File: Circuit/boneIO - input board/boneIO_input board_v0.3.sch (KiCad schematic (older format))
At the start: 274 parts, among them J1 Conn_02x04_Odd_Even, J10 Screw_Terminal_01x04, J11 Screw_Terminal_01x08, J12 BeagleBone_Black_Header, J13 ZW_VCC, J14 ZW_GND, J15 BeagleBone_Black_Header, J16 INNY ZASILACZ, J2 Screw_Terminal_01x08, J3 Screw_Terminal_01x08, J4 Screw_Terminal_01x08, J5 Screw_Terminal_01x08, J6 Screw_Terminal_01x08, J7 Screw_Terminal_01x08, J8 Screw_Terminal_01x08, J9 Screw_Terminal_01x08, SW1 SW_Push, U1 EL357N-G, U1 P82B96, U16 DS1307Z+, U17 TLP290-4, U6 LM2596S-ADJ, U7 RS485, Y1 32,788 MHz

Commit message: PCB design work
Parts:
- removed C55, C56, C57, C58: 100n, Capacitor_SMD:C_0603_1608Metric, symbol Device:C
- removed R108, R109, R110, R111: 4,7k, Resistor_SMD:R_0603_1608Metric, symbol Device:R
- removed R113, R114, R115, R116: 10k, Resistor_SMD:R_0603_1608Metric, symbol Device:R
- removed U17: TLP290-4, Package_SO:SOP-16_4.55x10.3mm_P1.27mm, symbol Isolator:TLP290-4
- U12, U13, U14, U15, U16, U17, U18, U19, U20, U21, U22, U23, U24, U25, U26, U27, U28, U29, U3, U30, U31, U32, U33, U34, U35, U37, U38, U39, U4, U40, U41, U42, U43, U44, U45, U46, U47, U48, U49, U5, U50, U51, U52, U53, U54, U55, U56, U6, U7, U8, U9: renamed from U?; value EL357N-G -> PC817X2NIP0F; footprint Package_SO:OPTO_EL357N-G -> boneIO - RM85:SOT254P975X400-4N
- U2: renamed from U1; value EL357N-G -> PC817X2NIP0F; footprint Package_SO:OPTO_EL357N-G -> boneIO - RM85:SOT254P975X400-4N
- gave numbers to parts that had none: 153
- renumbered C20 to C12, C21 to C13, C38 to C22, C22 to C4, J3 to J1, J2 to J10, J13 to J12, J14 to J13, J16 to J14, J12 to J15, J15 to J16, J4 to J2, J5 to J3, J6 to J4, J7 to J5, J8 to J6, J9 to J7, J10 to J8, J1 to J9, R26 to R10, R18 to R11, R35 to R19, R36 to R20, R37 to R29, R70 to R38, R71 to R39, R92 to R56, R97 to R57, R106 to R66, R107 to R67, R112 to R76, R17 to R9, U6 to U10, U7 to U11, U16 to U36
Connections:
- wire segments 954 -> 910
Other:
- moved on the sheet: ANVDD1, BT1, C1, C10, C11, C12, C13, C14, C15, C16, C17, C18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

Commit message: update PCB
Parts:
- J15, J16: symbol Connector_Generic:BeagleBone_Black_Header -> boneIO_input-board_v0.3-rescue:BeagleBone_Black_Header-Connector_Generic
- U11: symbol RF_Module:RS485 -> boneIO_input-board_v0.3-rescue:RS485-RF_Module
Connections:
- net P9,25 is gone; now on net P9.25: C42.1, R88.1, U40.4
- net P9.29_OUT: now also J6.7 (Pin_7); no longer J6.8 (Pin_8)
- net P9.30_OUT: now also J6.8 (Pin_8); no longer J6.7 (Pin_7)
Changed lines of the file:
@@
 P8.07_OUT
 $Comp
-L RF_Module:RS485 U11
+L boneIO_input-board_v0.3-rescue:RS485-RF_Module U11
 U 1 1 6187A9D0
 P 6350 4700
@@
 P8.39_OUT
 $Comp
-L Connector_Generic:BeagleBone_Black_Header J15
+L boneIO_input-board_v0.3-rescue:BeagleBone_Black_Header-Connector_Generic J15
 U 1 1 64765995
 P 27900 3650
@@
 $EndComp
 $Comp
-L Connector_Generic:BeagleBone_Black_Header J16
+L boneIO_input-board_v0.3-rescue:BeagleBone_Black_Header-Connector_Generic J16
 U 1 1 643393F0
 P 29900 3650
@@
 Text GLabel 6450 9100 2    50   Input ~ 0
 P9.31_OUT
-Text GLabel 6450 9200 2    50   Input ~ 0
-P9.30_OUT
 Text GLabel 6450 9300 2    50   Input ~ 0
+P9.30_OUT
+Text GLabel 6450 9200 2    50   Input ~ 0
 P9.29_OUT
 Text GLabel 8050 7600 2    50   Input ~ 0
@@
 $EndComp
 Text GLabel 17700 15900 2    50   Input ~ 0
-P9,25
+P9.25
 Wire Wire Line
 	16850 15900 17350 15900

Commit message: update PCB 08/11/21
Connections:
- net P9.07 is gone; now on net P8.07: C55.1, R113.1, U53.4
- net P9.24 is gone; now on net P8.13: C51.1, R105.1, U49.4
- net P9.26 is gone; now on net P8.19: C41.1, R87.1, U39.4
- net P8.07_OUT: now also J8.4 (Pin_4); no longer J6.4 (Pin_4)
- net P8.08_OUT: now also J8.3 (Pin_3), U31.2; no longer J6.3 (Pin_3), U35.2
- net P8.09_OUT: now also J8.2 (Pin_2), U32.2; no longer J6.2 (Pin_2), U34.2
- net P8.10_OUT: now also J6.8 (Pin_8); no longer J4.8 (Pin_8)
- net P8.11_OUT: now also J6.7 (Pin_7), U34.2; no longer J4.7 (Pin_7), U32.2
- net P8.12_OUT: now also J6.6 (Pin_6), U35.2; no longer J4.6 (Pin_6), U31.2
- net P8.14_OUT: now also J6.4 (Pin_4), U26.2; no longer J4.5 (Pin_5), U30.2
- net P8.15_OUT: now also J6.3 (Pin_3), U27.2; no longer J4.4 (Pin_4), U29.2
- net P8.16_OUT: now also J6.2 (Pin_2); no longer J4.3 (Pin_3)
- net P8.17_OUT: now also J4.8 (Pin_8), U30.2; no longer J4.2 (Pin_2), U27.2
- net P8.18_OUT: now also J4.7 (Pin_7), U29.2; no longer J2.8 (Pin_8), U26.2
- net P8.26_OUT: now also J4.5 (Pin_5); no longer J3.8 (Pin_8)
- net P8.27_OUT: now also J4.4 (Pin_4); no longer J3.7 (Pin_7)
- net P8.28_OUT: now also J4.3 (Pin_3); no longer J3.6 (Pin_6)
- net P8.29_OUT: now also J4.2 (Pin_2); no longer J3.5 (Pin_5)
- net P8.30_OUT: now also J2.8 (Pin_8); no longer J3.4 (Pin_4)
- net P8.31_OUT: now also J2.7 (Pin_7); no longer J3.3 (Pin_3)
- net P8.32_OUT: now also J2.6 (Pin_6); no longer J3.2 (Pin_2)
- net P8.33_OUT: now also J2.5 (Pin_5); no longer J1.8 (Pin_8)
- net P8.34_OUT: now also J2.4 (Pin_4); no longer J1.7 (Pin_7)
- net P8.35_OUT: now also J2.3 (Pin_3); no longer J1.6 (Pin_6)
- net P8.36_OUT: now also J2.2 (Pin_2); no longer J1.5 (Pin_5)
- net P8.37_OUT: now also J3.8 (Pin_8); no longer J1.4 (Pin_4)
- net P8.38_OUT: now also J3.7 (Pin_7); no longer J1.3 (Pin_3)
- net P8.39_OUT: now also J3.6 (Pin_6); no longer J1.2 (Pin_2)
- net P8.40_OUT: now also J3.5 (Pin_5); no longer J5.8 (Pin_8)
- net P8.41_OUT: now also J3.4 (Pin_4); no longer J5.7 (Pin_7)
- net P8.42_OUT: now also J3.3 (Pin_3); no longer J5.6 (Pin_6)
- net P8.43_OUT: now also J3.2 (Pin_2); no longer J5.5 (Pin_5)
- net P8.44_OUT: now also J1.8 (Pin_8); no longer J5.4 (Pin_4)
- net P8.45_OUT: now also J1.7 (Pin_7); no longer J5.3 (Pin_3)
- net P8.46_OUT: now also J1.6 (Pin_6); no longer J5.2 (Pin_2)
- net P9.11_OUT: now also J7.2 (Pin_2); no longer J2.2 (Pin_2)
- net P9.12_OUT: now also J7.3 (Pin_3); no longer J2.3 (Pin_3)
- net P9.13_OUT: now also J7.4 (Pin_4); no longer J2.4 (Pin_4)
- net P9.14_OUT: now also J7.5 (Pin_5); no longer J2.5 (Pin_5)
- net P9.15_OUT: now also J7.6 (Pin_6); no longer J2.6 (Pin_6)
- net P9.16_OUT: now also J7.7 (Pin_7); no longer J2.7 (Pin_7)
- net P9.18_OUT: now also J5.2 (Pin_2); no longer J8.2 (Pin_2)
- net P9.21_OUT: now also J5.3 (Pin_3); no longer J8.3 (Pin_3)
- net P9.22_OUT: now also J5.4 (Pin_4); no longer J8.4 (Pin_4)
- net P9.23_OUT: now also J5.5 (Pin_5); no longer J7.7 (Pin_7)
- net P9.25_OUT: now also J5.6 (Pin_6); no longer J7.5 (Pin_5)
- net P9.27_OUT: now also J5.7 (Pin_7); no longer J7.3 (Pin_3)
- net P9.28_OUT: now also J5.8 (Pin_8); no longer J7.2 (Pin_2)
- net P9.29_OUT: now also J1.2 (Pin_2); no longer J6.7 (Pin_7)
- net P9.30_OUT: now also J1.3 (Pin_3); no longer J6.8 (Pin_8)
- net P9.31_OUT: now also J1.4 (Pin_4); no longer J6.6 (Pin_6)
- net P9.42_OUT: now also J1.5 (Pin_5); no longer J6.5 (Pin_5)
- net P9.24_OUT renamed P8.13_OUT
- net P8.13_OUT: now also J6.5 (Pin_5); no longer J7.6 (Pin_6)
- net P9.26_OUT renamed P8.19_OUT
- net P8.19_OUT: now also J4.6 (Pin_6); no longer J7.4 (Pin_4)
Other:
- moved on the sheet: C26, C27, C28, C29, C30, C31, C32, C33, C34, C35, C36, C37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

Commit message: PCB board to be checked
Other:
- note added: "ADC\n\n\n"
- note added: "Input Board v0.2 BBB\n\n\n"
- note added: "Jumper\n\n\n\n"
- note added: "PinOut\n\n\n\n"
- note added: "RS485\n\n\n\n"
- note added: "Transoptors\n\n\n\n"
- moved on the sheet: ANVDD1, BT1, C1, C10, C11, C12, C13, C14, C15, C16, C17, C18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

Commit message: update PCB
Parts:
- D5: JLCPCB (none) -> C68883
- R1, R100, R109, R110, R111, R112, R2, R21, R22, R23, R24, R25, R26, R27, R28, R3, R4, R40, R41, R42, R43, R44, R45, R46, R47, R5, R58, R59, R6, R60, R61, R62, R63, R64, R65, R7, R77, R78, R79, R8, R80, R81, R82, R83, R84, R93, R94, R95, R96, R97, R98, R99: JLCPCB C238881 -> C237118
- R39, R56, R57: JLCPCB C101062 -> C237118
- U1: JLCPCB (none) -> C32103

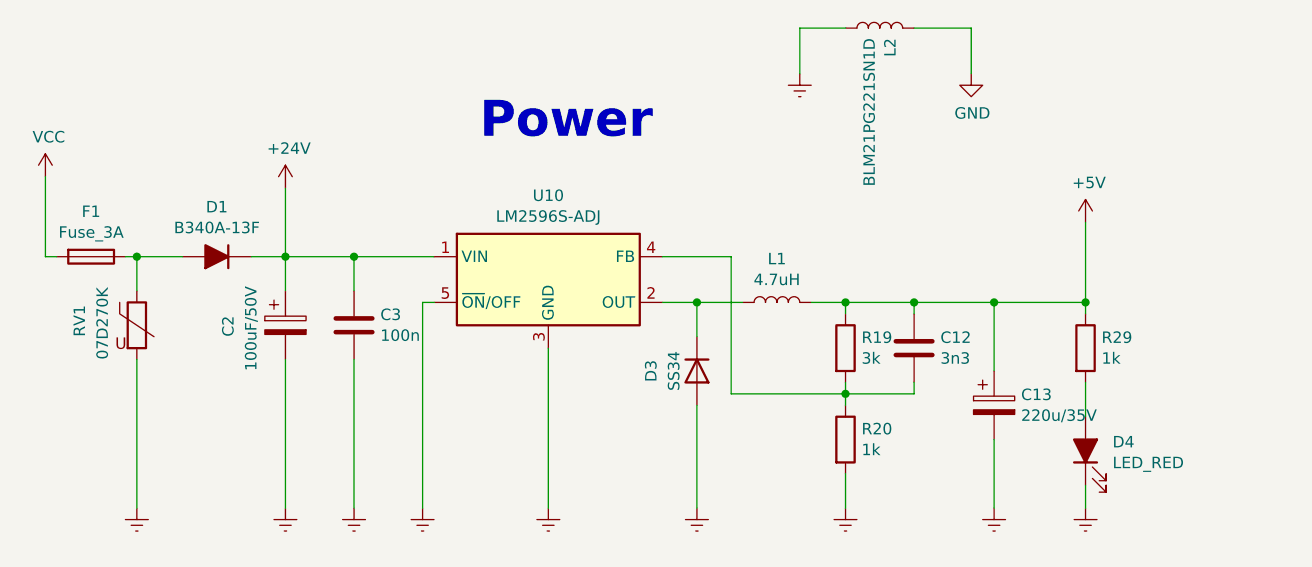
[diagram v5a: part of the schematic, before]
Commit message: update
zmiany w rozmieszczeniu BBB i dodane Gerbery, BOM i P&P
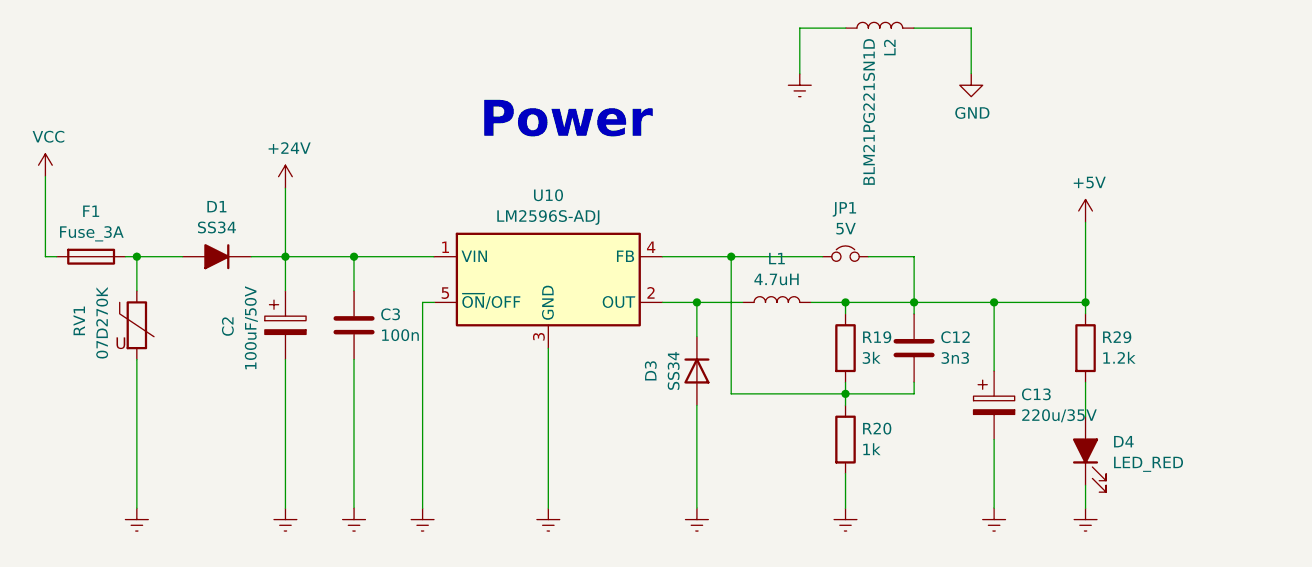
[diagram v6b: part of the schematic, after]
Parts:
- added JP1: 5V, Jumper:SolderJumper-2_P1.3mm_Open_Pad1.0x1.5mm, symbol Device:Jumper_NC_Small
- D1: value B340A-13F -> SS34
- R29: value 1k -> 1.2k
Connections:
- net +5V: now also JP1.2
- net at C12.2, R19.2, R20.1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: now also JP1.1
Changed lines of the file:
@@
 P 6800 5950
 F 0 "R29" H 6870 5996 50  0000 L CNN
-F 1 "1k" H 6870 5905 50  0000 L CNN
+F 1 "1.2k" H 6870 5905 50  0000 L CNN
 F 2 "Resistor_SMD:R_0603_1608Metric" V 6730 5950 50  0001 C CNN
 F 3 "~" H 6800 5950 50  0001 C CNN
@@
 P 3000 5550
 F 0 "D1" H 3000 5333 50  0000 C CNN
-F 1 "B340A-13F" H 3000 5424 50  0000 C CNN
+F 1 "SS34" H 3000 5424 50  0000 C CNN
 F 2 "Diode_SMD:D_SMA" H 3000 5550 50  0001 C CNN
 F 3 "~" H 3000 5550 50  0001 C CNN
@@
 Text Notes 12050 4200 0    394  ~ 79
 Input Board v0.2 BBB\n\n\n
+$Comp
+L Device:Jumper_NC_Small JP1
+U 1 1 61979A0C
+P 5750 5550
+F 0 "JP1" H 5750 5762 50  0000 C CNN
+F 1 "5V" H 5750 5671 50  0000 C CNN
+F 2 "Jumper:SolderJumper-2_P1.3mm_Open_Pad1.0x1.5mm" H 5750 5550 50  0001 C CNN
+F 3 "~" H 5750 5550 50  0001 C CNN
+	1    5750 5550
+	1    0    0    -1
+$EndComp
+Wire Wire Line
+	5250 5550 5650 5550
+Connection ~ 5250 5550
+Wire Wire Line
+	6050 5750 6050 5550
+Wire Wire Line
+	6050 5550 5850 5550
 $EndSCHEMATC

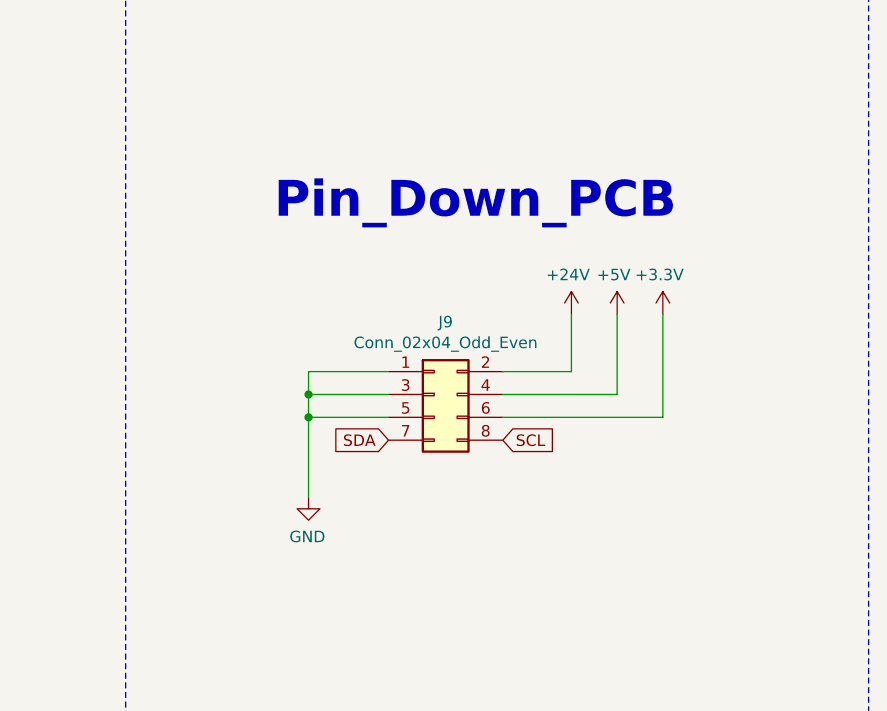
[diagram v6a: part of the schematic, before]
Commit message: Wymiana gniazda
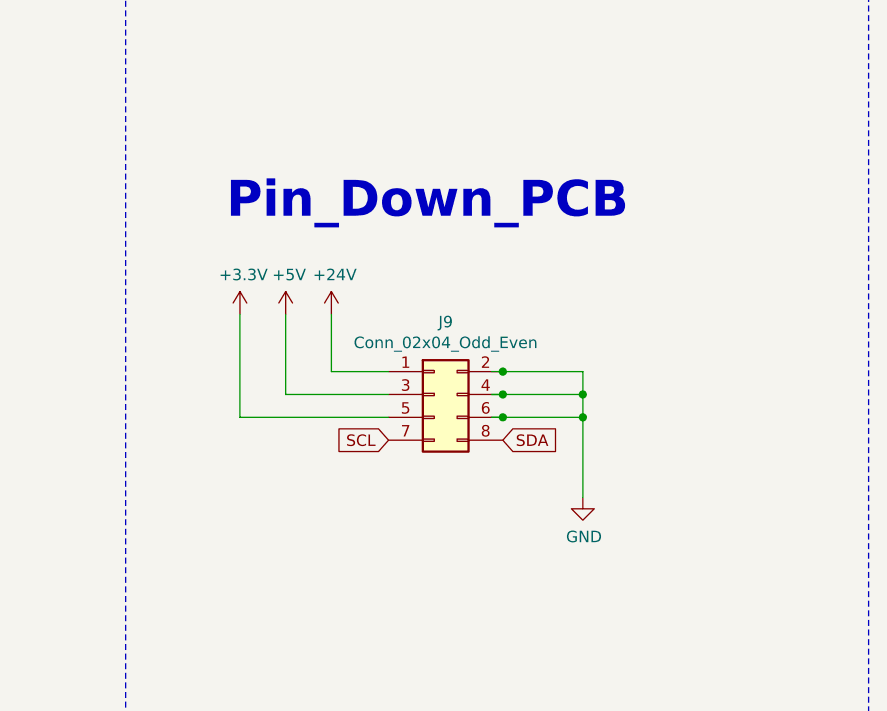
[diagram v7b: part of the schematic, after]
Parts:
- J9: footprint Connector_PinHeader_2.54mm:PinHeader_2x04_P2.54mm_Vertical -> Connector_PinSocket_2.54mm:PinSocket_2x04_P2.54mm_Vertical
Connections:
- net +24V: now also J9.1 (Pin_1); no longer J9.2 (Pin_2)
- net +3V3: now also J9.5 (Pin_5); no longer J9.6 (Pin_6)
- net +5V: now also J9.3 (Pin_3); no longer J9.4 (Pin_4)
- net GND: now also J9.2 (Pin_2), J9.4 (Pin_4), J9.6 (Pin_6); no longer J9.1 (Pin_1), J9.3 (Pin_3), J9.5 (Pin_5)
- net SCL: now also J9.7 (Pin_7); no longer J9.8 (Pin_8)
- net SDA: now also J9.8 (Pin_8); no longer J9.7 (Pin_7)
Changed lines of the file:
@@
 F 0 "J9" H 30250 17217 50  0000 C CNN
 F 1 "Conn_02x04_Odd_Even" H 30250 17126 50  0000 C CNN
-F 2 "Connector_PinHeader_2.54mm:PinHeader_2x04_P2.54mm_Vertical" H 30200 16900 50  0001 C CNN
+F 2 "Connector_PinSocket_2.54mm:PinSocket_2x04_P2.54mm_Vertical" H 30200 16900 50  0001 C CNN
 F 3 "~" H 30200 16900 50  0001 C CNN
 	1    30200 16900
@@
 L power:+24V #PWR0118
 U 1 1 61857D08
-P 30800 16550
-F 0 "#PWR0118" H 30800 16400 50  0001 C CNN
-F 1 "+24V" H 30815 16723 50  0000 C CNN
-F 2 "" H 30800 16550 50  0001 C CNN
-F 3 "" H 30800 16550 50  0001 C CNN
-	1    30800 16550
-	-1   0    0    -1
+P 29750 16550
+F 0 "#PWR0118" H 29750 16400 50  0001 C CNN
+F 1 "+24V" H 29765 16723 50  0000 C CNN
+F 2 "" H 29750 16550 50  0001 C CNN
+F 3 "" H 29750 16550 50  0001 C CNN
+	1    29750 16550
+	1    0    0    -1
 $EndComp
 $Comp
 L power:+5V #PWR0119
 U 1 1 61859D3B
-P 31000 16550
-F 0 "#PWR0119" H 31000 16400 50  0001 C CNN
-F 1 "+5V" H 31015 16723 50  0000 C CNN
-F 2 "" H 31000 16550 50  0001 C CNN
-F 3 "" H 31000 16550 50  0001 C CNN
-	1    31000 16550
-	-1   0    0    -1
+P 29550 16550
+F 0 "#PWR0119" H 29550 16400 50  0001 C CNN
+F 1 "+5V" H 29565 16723 50  0000 C CNN
+F 2 "" H 29550 16550 50  0001 C CNN
+F 3 "" H 29550 16550 50  0001 C CNN
+	1    29550 16550
+	1    0    0    -1
 $EndComp
 $Comp
 L power:+3.3V #PWR0136
 U 1 1 6185BCCA
-P 31200 16550
-F 0 "#PWR0136" H 31200 16400 50  0001 C CNN
-F 1 "+3.3V" H 31215 16723 50  0000 C CNN
-F 2 "" H 31200 16550 50  0001 C CNN
-F 3 "" H 31200 16550 50  0001 C CNN
-	1    31200 16550
-	-1   0    0    -1
+P 29350 16550
+F 0 "#PWR0136" H 29350 16400 50  0001 C CNN
+F 1 "+3.3V" H 29365 16723 50  0000 C CNN
+F 2 "" H 29350 16550 50  0001 C CNN
+F 3 "" H 29350 16550 50  0001 C CNN
+	1    29350 16550
+	1    0    0    -1
 $EndComp
 Wire Wire Line
-	30500 16800 30800 16800
+	30450 16800 30500 16800
 Wire Wire Line
-	30800 16800 30800 16550
+	29750 16800 29750 16550
 Wire Wire Line
-	30500 16900 31000 16900
+	30450 16900 30500 16900
 Wire Wire Line
-	31000 16900 31000 16550
+	29550 16900 29550 16550
 Wire Wire Line
-	30500 17000 31200 17000
+	30450 17000 30500 17000
 Wire Wire Line
-	30000 17000 29650 17000
+	30500 17000 30850 17000
 Wire Wire Line
-	30000 16800 29650 16800
+	30500 16800 30850 16800
 Wire Wire Line
-	29650 16800 29650 16900
+	30850 16800 30850 16900
 Wire Wire Line
-	30000 16900 29650 16900
-Connection ~ 29650 16900
-Text GLabel 30000 17100 0    50   Input ~ 0
-SDA
+	30500 16900 30850 16900
+Connection ~ 30850 16900
 Text GLabel 30500 17100 2    50   Input ~ 0
+SDA
+Text GLabel 30000 17100 0    50   Input ~ 0
 SCL
-Text Notes 29500 16400 0    157  ~ 31
+Text Notes 31050 16400 2    157  ~ 31
 Pin_Down_PCB\n\n
 Wire Wire Line
-	29650 16900 29650 17000
+	30850 16900 30850 17000
 Wire Wire Line
-	31200 17000 31200 16550
+	29350 17000 29350 16550
 $Comp
 L Connector:Screw_Terminal_01x08 J7
@@
 	20750 5300 20750 5700
 Wire Wire Line
-	29650 17000 29650 17350
+	30850 17000 30850 17350
 $Comp
 L power:GND #PWR0109
 U 1 1 61C1E0E6
-P 29650 17350
-F 0 "#PWR0109" H 29650 17100 50  0001 C CNN
-F 1 "GND" H 29655 17177 50  0000 C CNN
-F 2 "" H 29650 17350 50  0001 C CNN
-F 3 "" H 29650 17350 50  0001 C CNN
-	1    29650 17350
-	-1   0    0    -1
+P 30850 17350
+F 0 "#PWR0109" H 30850 17100 50  0001 C CNN
+F 1 "GND" H 30855 17177 50  0000 C CNN
+F 2 "" H 30850 17350 50  0001 C CNN
+F 3 "" H 30850 17350 50  0001 C CNN
+	1    30850 17350
+	1    0    0    -1
 $EndComp
-Connection ~ 29650 17000
+Connection ~ 30850 17000
 $Comp
 L Connector:Screw_Terminal_01x08 J5
@@
 Wire Wire Line
 	6050 5550 5850 5550
+Wire Wire Line
+	30000 16800 29750 16800
+Wire Wire Line
+	30000 16900 29550 16900
+Wire Wire Line
+	30000 17000 29350 17000
+Connection ~ 30500 16800
+Connection ~ 30500 16900
+Connection ~ 30500 17000
 $EndSCHEMATC
